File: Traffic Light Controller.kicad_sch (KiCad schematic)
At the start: 64 parts, among them J1 Conn_02x08_Odd_Even, J2 Conn_02x08_Odd_Even, J3 Conn_02x05_Odd_Even, J4 +5V, SW1 RST, SW2 OVR, SW3 EN, U1 SM420561N, U2 SM420561N, U3 LM1117DT-3.3

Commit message: update
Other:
- note added: "EMERGENCY OVERRIDE"
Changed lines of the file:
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@@
 	)
 	(rectangle
-		(start 190.246 35.56)
+		(start 190.246 34.544)
 		(end 279.146 147.574)
 		(stroke
@@
 	(text "CONTROL LOGIC"
 		(exclude_from_sim no)
-		(at 198.12 34.544 0)
+		(at 198.12 32.766 0)
 		(effects
 			(font
@@
 		)
 	)
-	(text "ENABLE"
-		(exclude_from_sim no)
-		(at 195.834 76.454 0)
-		(effects
-			(font
+	(text "EMERGENCY OVERRIDE"
+		(exclude_from_sim no)
+		(at 202.438 76.2 0)
+		(effects
+			(font

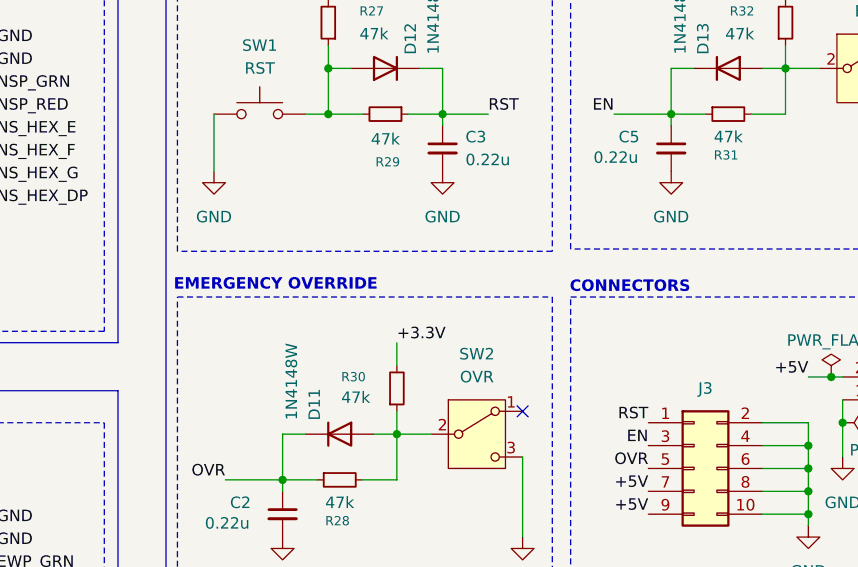
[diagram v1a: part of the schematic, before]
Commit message: converted to 9.0 version
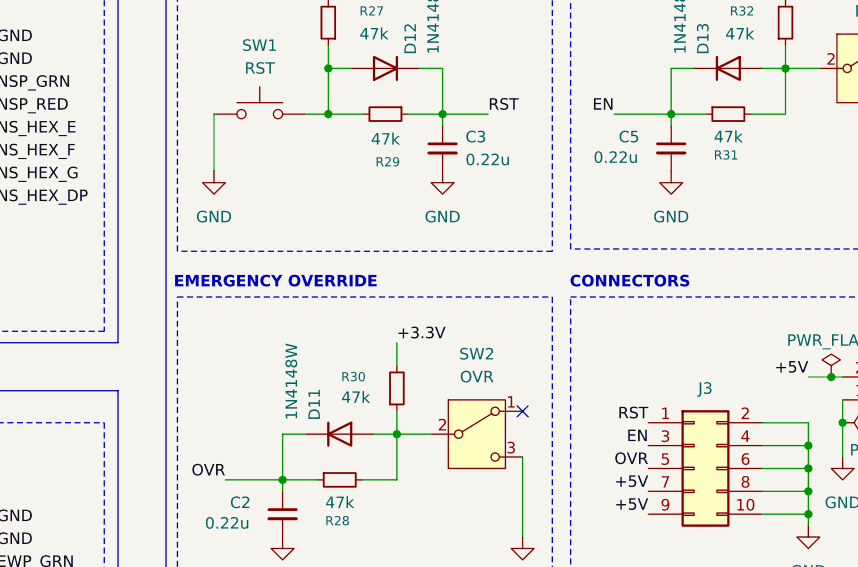
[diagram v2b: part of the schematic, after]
